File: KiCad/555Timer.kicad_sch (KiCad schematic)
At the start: 6 parts, among them U3 NE555P

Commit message: minor fixes
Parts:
- C1: footprint (none) -> Capacitor_THT:C_Disc_D5.0mm_W2.5mm_P5.00mm; Distributor (none) -> https://www.mouser.de/ProductDetail/TDK/FK28X5R0J105K?qs=zL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
- C2: footprint (none) -> Capacitor_THT:C_Disc_D5.0mm_W2.5mm_P5.00mm
- R1: footprint (none) -> Resistor_THT:R_Axial_DIN0207_L6.3mm_D2.5mm_P7.62mm_Horizontal
- RV1: footprint (none) -> poti_rv09a:RV09AF-40-ALPHA-POT; DIstributor (none) -> https://www.mouser.de/ProductDetail/Amphenol-Piher/PT10MV10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
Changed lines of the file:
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@@
       (effects (font (size 1.27 1.27)) (justify left))
     )
-    (property "Footprint" "" (at 172.4152 97.79 0)
+    (property "Footprint" "Capacitor_THT:C_Disc_D5.0mm_W2.5mm_P5.00mm" (at 172.4152 97.79 0)
       (effects (font (size 1.27 1.27)) hide)
     )
@@
       (effects (font (size 1.27 1.27)) (justify left))
     )
-    (property "Footprint" "" (at 112.0648 123.19 0)
-      (effects (font (size 1.27 1.27)) hide)
-    )
-    (property "Datasheet" "~" (at 113.03 127 0)
+    (property "Footprint" "Capacitor_THT:C_Disc_D5.0mm_W2.5mm_P5.00mm" (at 112.0648 123.19 0)
+      (effects (font (size 1.27 1.27)) hide)
+    )
+    (property "Datasheet" "https://product.tdk.com/en/system/files?file=dam/doc/product/capacitor/ceramic/lead-mlcc/catalog/leadmlcc_conventional_fk_en.pdf" (at 113.03 127 0)
+      (effects (font (size 1.27 1.27)) hide)
+    )
+    (property "Distributor" "https://www.mouser.de/ProductDetail/TDK/FK28X5R0J105K?qs=zLBlM7QTTNrG4I3PJ1W9Pg%3D%3D" (at 113.03 127 0)
       (effects (font (size 1.27 1.27)) hide)
     )
@@
       (effects (font (size 1.27 1.27)) (justify right))
     )
-    (property "Footprint" "" (at 113.03 96.52 0)
+    (property "Footprint" "poti_rv09a:RV09AF-40-ALPHA-POT" (at 113.03 96.52 0)
       (effects (font (size 1.27 1.27)) hide)
     )
@@
       (effects (font (size 1.27 1.27)) hide)
     )
+    (property "DIstributor" "https://www.mouser.de/ProductDetail/Amphenol-Piher/PT10MV10-105B2020-PM-S?qs=t7xnP681wgVwo%252BS7b%2FwjCw%3D%3D" (at 113.03 96.52 0)
+      (effects (font (size 1.27 1.27)) hide)
+    )
     (pin "1")
     (pin "2")
@@
       (effects (font (size 1.27 1.27)) (justify left))
     )
-    (property "Footprint" "" (at 120.3452 123.19 0)
+    (property "Footprint" "Capacitor_THT:C_Disc_D5.0mm_W2.5mm_P5.00mm" (at 120.3452 123.19 0)
       (effects (font (size 1.27 1.27)) hide)
     )
@@
       (effects (font (size 1.27 1.27)) (justify right))
     )
-    (property "Footprint" "" (at 111.252 88.9 90)
-      (effects (font (size 1.27 1.27)) hide)
-    )
+    (property "Footprint" "Resistor_THT:R_Axial_DIN0207_L6.3mm_D2.5mm_P7.62mm_Horizontal" (at 111.252 88.9 90)
+      (effects (font (size 1.27 1.27)) hide)
+    )

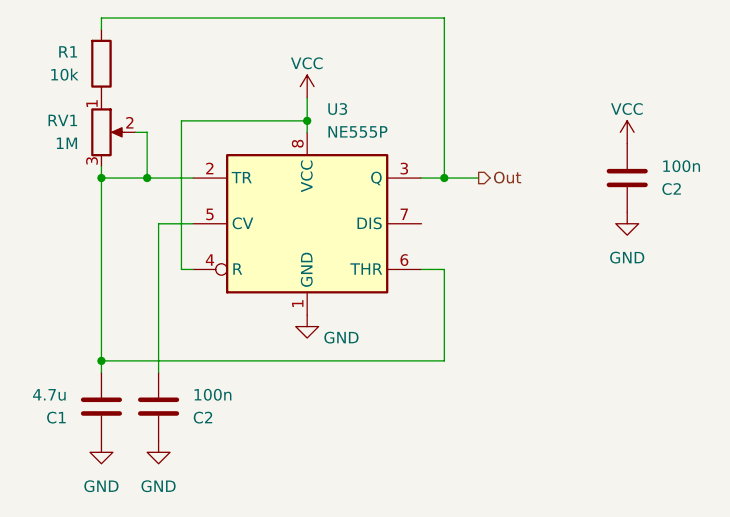
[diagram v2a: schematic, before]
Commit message: switch Poti wiring, adjust to JLCPCB design rules
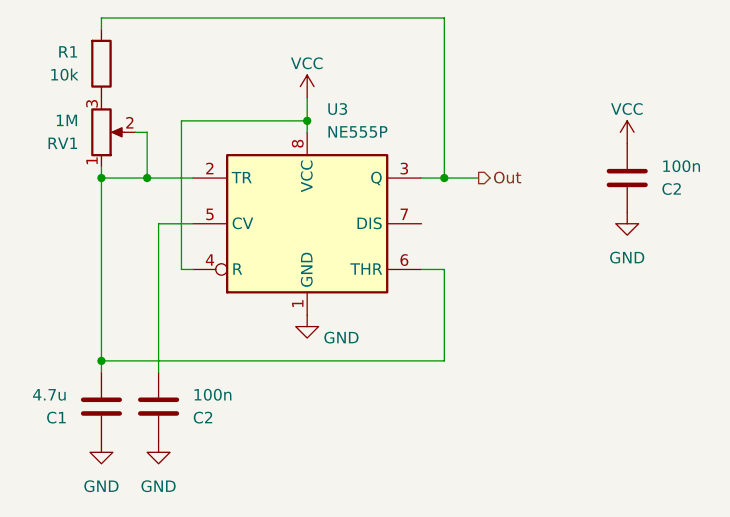
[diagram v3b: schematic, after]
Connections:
- net at C1.2, RV1.2, U3.2 (TR)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: now also RV1.1; no longer RV1.3
- net at R1.1: now also RV1.3; no longer RV1.1
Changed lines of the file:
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@@
     )
   )
-  (symbol (lib_id "Device:R_Potentiometer") (at 113.03 96.52 0) (unit 1)
-    (in_bom yes) (on_board yes) (dnp no) (fields_autoplaced)
-    (property "Reference" "RV1" (at 110.49 95.25 0)
+  (symbol (lib_id "Device:R_Potentiometer") (at 113.03 96.52 0) (mirror x) (unit 1)
+    (in_bom yes) (on_board yes) (dnp no)
+    (property "Reference" "RV1" (at 110.49 97.79 0)
       (effects (font (size 1.27 1.27)) (justify right))
     )
-    (property "Value" "1M" (at 110.49 97.79 0)
+    (property "Value" "1M" (at 110.49 95.25 0)
       (effects (font (size 1.27 1.27)) (justify right))
     )
